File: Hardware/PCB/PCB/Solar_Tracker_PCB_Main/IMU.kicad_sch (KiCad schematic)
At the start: 11 parts, among them IC3 BNO085, Y1 32.768kHz

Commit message: Actualizacion Main pcb
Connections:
- net IMU_CLKSEL0: no longer names the net of IC3.10 (CLKSEL0)
- no-connect marks 12 -> 13
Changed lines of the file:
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@@
+	)
+	(no_connect
+		(at 33.02 124.46)
 	)
 	(no_connect
@@
 				(hide yes)
 			)
-		)
-	)
-	(global_label "IMU_CLKSEL0"
-		(shape input)
-		(at 33.02 124.46 180)
-		(fields_autoplaced yes)
-		(effects
-			(font
-				(size 1.27 1.27)
-			)
-			(justify right)
-		)
-		(property "Intersheetrefs" "${INTERSHEET_REFS}"
-			(at 17.5163 124.46 0)
-			(effects
-				(font
-					(size 1.27 1.27)
-				)
-				(justify right)
-				(hide yes)
-			)

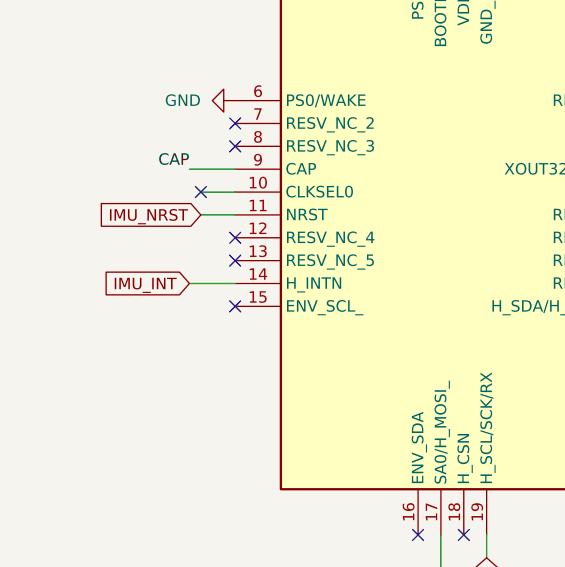
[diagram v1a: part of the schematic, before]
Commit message: Modificaciones PCB MAIN
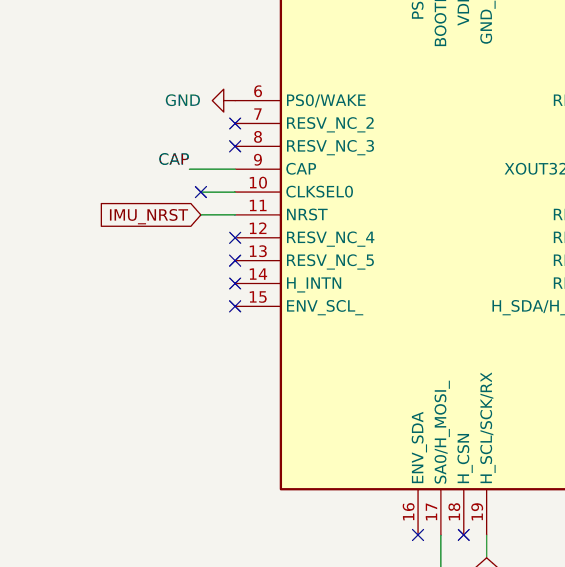
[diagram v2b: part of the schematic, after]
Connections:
- net IMU_INT: no longer names the net of IC3.14 (H_INTN)
- no-connect marks 13 -> 14
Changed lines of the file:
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@@
+	)
+	(no_connect
+		(at 36.83 134.62)
 	)
 	(no_connect
@@
 		(pts
 			(xy 102.87 25.4) (xy 93.98 25.4)
-		)
-		(stroke
-			(width 0)
-			(type default)
-		)
-	)
-	(wire
-		(pts
-			(xy 31.75 134.62) (xy 36.83 134.62)
 		)
 		(stroke
@@
 				(hide yes)
 			)
-		)
-	)
-	(global_label "IMU_INT"
-		(shape input)
-		(at 31.75 134.62 180)
-		(fields_autoplaced yes)
-		(effects
-			(font
-				(size 1.27 1.27)
-			)
-			(justify right)
-		)
-		(property "Intersheetrefs" "${INTERSHEET_REFS}"
-			(at 21.5076 134.62 0)
-			(effects
-				(font
-					(size 1.27 1.27)
-				)
-				(justify right)
-				(hide yes)
-			)
